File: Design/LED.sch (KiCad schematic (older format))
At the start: 6 parts

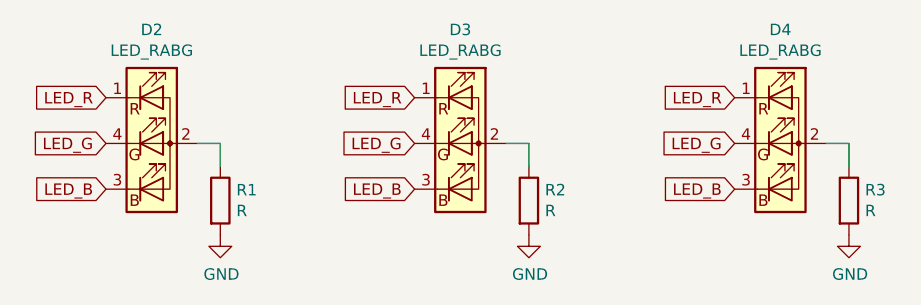
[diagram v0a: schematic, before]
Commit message: Improvement over the Power management: - added TPS6201DRC for raising leaking voltage from supercapacitor - supercap is protected from overvoltage using a shunt diode - power management is using MOSFET logic (2 PFET, 1 NFET)
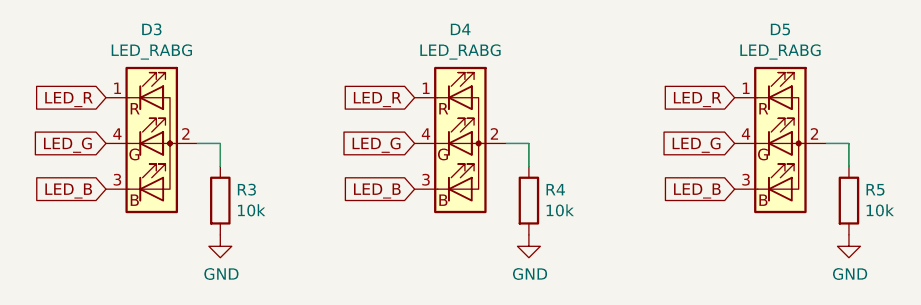
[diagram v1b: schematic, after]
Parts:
- R3: renamed from R1; value R -> 10k
- R4: renamed from R2; value R -> 10k
- R5: renamed from R3; value R -> 10k
- renumbered D2 to D3, D3 to D4, D4 to D5
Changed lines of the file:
@@
 P 2000 1650
 AR Path="/5E136FFE" Ref="R?"  Part="1"
-AR Path="/5E12D0D3/5E136FFE" Ref="R1"  Part="1"
-F 0 "R1" H 2070 1696 50  0000 L CNN
-F 1 "R" H 2070 1605 50  0000 L CNN
+AR Path="/5E12D0D3/5E136FFE" Ref="R3"  Part="1"
+F 0 "R3" H 2070 1696 50  0000 L CNN
+F 1 "10k" H 2070 1605 50  0000 L CNN
 F 2 "" V 1930 1650 50  0001 C CNN
 F 3 "~" H 2000 1650 50  0001 C CNN
@@
 P 2000 1800
 AR Path="/5E13700A" Ref="#PWR?"  Part="1"
-AR Path="/5E12D0D3/5E13700A" Ref="#PWR07"  Part="1"
-F 0 "#PWR07" H 2000 1550 50  0001 C CNN
+AR Path="/5E12D0D3/5E13700A" Ref="#PWR09"  Part="1"
+F 0 "#PWR09" H 2000 1550 50  0001 C CNN
 F 1 "GND" H 2005 1627 50  0000 C CNN
 F 2 "" H 2000 1800 50  0001 C CNN
@@
 P 1700 1400
 AR Path="/5E136FF8" Ref="D?"  Part="1"
-AR Path="/5E12D0D3/5E136FF8" Ref="D2"  Part="1"
-F 0 "D2" H 1700 1897 50  0000 C CNN
+AR Path="/5E12D0D3/5E136FF8" Ref="D3"  Part="1"
+F 0 "D3" H 1700 1897 50  0000 C CNN
 F 1 "LED_RABG" H 1700 1806 50  0000 C CNN
 F 2 "LED_D5.0mm-4" H 1700 1350 50  0001 C CNN
@@
 P 3350 1650
 AR Path="/5E1D1BE5" Ref="R?"  Part="1"
-AR Path="/5E12D0D3/5E1D1BE5" Ref="R2"  Part="1"
-F 0 "R2" H 3420 1696 50  0000 L CNN
-F 1 "R" H 3420 1605 50  0000 L CNN
+AR Path="/5E12D0D3/5E1D1BE5" Ref="R4"  Part="1"
+F 0 "R4" H 3420 1696 50  0000 L CNN
+F 1 "10k" H 3420 1605 50  0000 L CNN
 F 2 "" V 3280 1650 50  0001 C CNN
 F 3 "~" H 3350 1650 50  0001 C CNN
@@
 P 3350 1800
 AR Path="/5E1D1BEF" Ref="#PWR?"  Part="1"
-AR Path="/5E12D0D3/5E1D1BEF" Ref="#PWR06"  Part="1"
-F 0 "#PWR06" H 3350 1550 50  0001 C CNN
+AR Path="/5E12D0D3/5E1D1BEF" Ref="#PWR010"  Part="1"
+F 0 "#PWR010" H 3350 1550 50  0001 C CNN
 F 1 "GND" H 3355 1627 50  0000 C CNN
 F 2 "" H 3350 1800 50  0001 C CNN
@@
 P 3050 1400
 AR Path="/5E1D1BFC" Ref="D?"  Part="1"
-AR Path="/5E12D0D3/5E1D1BFC" Ref="D3"  Part="1"
-F 0 "D3" H 3050 1897 50  0000 C CNN
+AR Path="/5E12D0D3/5E1D1BFC" Ref="D4"  Part="1"
+F 0 "D4" H 3050 1897 50  0000 C CNN
 F 1 "LED_RABG" H 3050 1806 50  0000 C CNN
 F 2 "LED_D5.0mm-4" H 3050 1350 50  0001 C CNN
@@
 P 4450 1400
 AR Path="/5E1D5989" Ref="D?"  Part="1"
-AR Path="/5E12D0D3/5E1D5989" Ref="D4"  Part="1"
-F 0 "D4" H 4450 1897 50  0000 C CNN
+AR Path="/5E12D0D3/5E1D5989" Ref="D5"  Part="1"
+F 0 "D5" H 4450 1897 50  0000 C CNN
 F 1 "LED_RABG" H 4450 1806 50  0000 C CNN
 F 2 "LED_D5.0mm-4" H 4450 1350 50  0001 C CNN
@@
 P 4750 1800
 AR Path="/5E1D597C" Ref="#PWR?"  Part="1"
-AR Path="/5E12D0D3/5E1D597C" Ref="#PWR010"  Part="1"
-F 0 "#PWR010" H 4750 1550 50  0001 C CNN
+AR Path="/5E12D0D3/5E1D597C" Ref="#PWR011"  Part="1"
+F 0 "#PWR011" H 4750 1550 50  0001 C CNN
 F 1 "GND" H 4755 1627 50  0000 C CNN
 F 2 "" H 4750 1800 50  0001 C CNN
@@
 P 4750 1650
 AR Path="/5E1D5972" Ref="R?"  Part="1"
-AR Path="/5E12D0D3/5E1D5972" Ref="R3"  Part="1"
-F 0 "R3" H 4820 1696 50  0000 L CNN
-F 1 "R" H 4820 1605 50  0000 L CNN
+AR Path="/5E12D0D3/5E1D5972" Ref="R5"  Part="1"
+F 0 "R5" H 4820 1696 50  0000 L CNN
+F 1 "10k" H 4820 1605 50  0000 L CNN
 F 2 "" V 4680 1650 50  0001 C CNN
 F 3 "~" H 4750 1650 50  0001 C CNN

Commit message: - designed configurable intensity for RGB LEDs - included Breakout (FET, Diode, etc.) Spice models from Cadence Spice - replaced global label with hierarchical complete view - customized net labels with pin function - exported first spice netlist which presents small bugs
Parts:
- removed R3: 10k, symbol Device:R
- added C19: 100nF, symbol Device:C
- added Q10, Q5, Q6, Q7, Q8, Q9: Q_NMOS_DGS, symbol Device:Q_NMOS_DGS
- added R8: 10k, symbol Device:R
- D2: renamed from D3; value LED_RABG -> LED_RGB; symbol Device:LED_RABG -> Device:LED_RGB; Spice_Lib_File (none) -> C:\\Cadence\\SPB_17.2\\tools\\pspice\\library\\breakout.lib; Spice_Model (none) -> DBreak; Spice_Netlist_Enabled (none) -> Y; Spice_Primitive (none) -> D
- D3: renamed from D4; value LED_RABG -> LED_RGB; symbol Device:LED_RABG -> Device:LED_RGB; Spice_Lib_File (none) -> C:\\Cadence\\SPB_17.2\\tools\\pspice\\library\\breakout.lib; Spice_Model (none) -> DBreak; Spice_Netlist_Enabled (none) -> Y; Spice_Primitive (none) -> D
- D4: renamed from D5; value LED_RABG -> LED_RGB; symbol Device:LED_RABG -> Device:LED_RGB; Spice_Lib_File (none) -> C:\\Cadence\\SPB_17.2\\tools\\pspice\\library\\breakout.lib; Spice_Model (none) -> DBreak; Spice_Netlist_Enabled (none) -> Y; Spice_Primitive (none) -> D
- renumbered R5 to R10, R4 to R9
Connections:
- net at D2.2 (GK): now also D2.1 (RK), D2.3 (BK), R8.1
- net at D3.2 (GK): now also D3.1 (RK), D3.3 (BK), R9.2; no longer R9.1
- net at D4.2 (GK): now also D4.1 (RK), D4.3 (BK), R10.2; no longer R10.1
- removed net GND: R10.2, R9.2
- removed net LED_B: D2.3 (BK), D3.3 (BK), D4.3 (BK)
- net LED_G: no longer names the net of D2.4 (BA), D3.4 (BA), D4.4 (BA)
- net LED_G: now also Q7.1 (D)
- removed net LED_R: D2.1 (RK), D3.1 (RK), D4.1 (RK)
- new net: D2.5 (GA), D3.5 (GA), D4.5 (GA), Q6.1 (D)
- new net: D2.6 (RA), D3.6 (RA), D4.6 (RA), Q5.1 (D)
- new net: Q5.2 (G), Q8.3 (S)
- new net: Q6.2 (G), Q9.3 (S)
- new net: Q10.3 (S), Q7.2 (G)
- new net 0: C19.2, Q5.3 (S), Q6.3 (S), Q7.3 (S)
- new net CPU_LED_Blink: C19.1, Q10.1 (D), Q8.1 (D), Q9.1 (D)
- new net LED_PWM_B: Q10.2 (G)
- new net LED_PWM_G: Q9.2 (G)
- new net LED_PWM_R: Q8.2 (G)
- new net VDD: R10.1, R8.2, R9.1
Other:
- moved on the sheet: R?
